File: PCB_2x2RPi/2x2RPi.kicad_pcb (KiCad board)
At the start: 2 copper layers, 44.4 x 53.3 mm, 31 parts, among them J1 USB, P1 VIN, P2 CONN_13X2, P3 INPUT, P4 REL2, P6 REL1, SW1 PWR SW, U1 LowCurVReg, U2 LowCurVReg, U3 TLP2531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

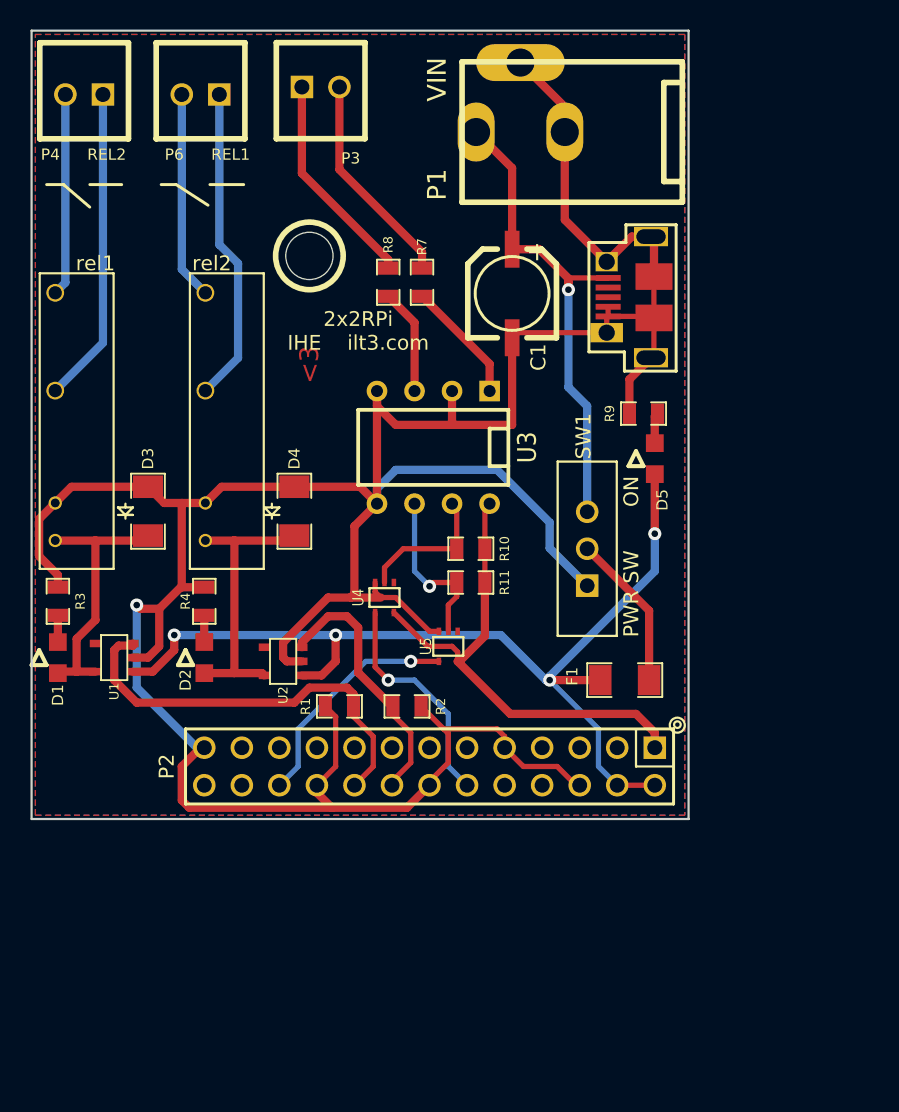
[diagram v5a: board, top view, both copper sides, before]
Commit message: Recreating schematic files, updating serial numbers
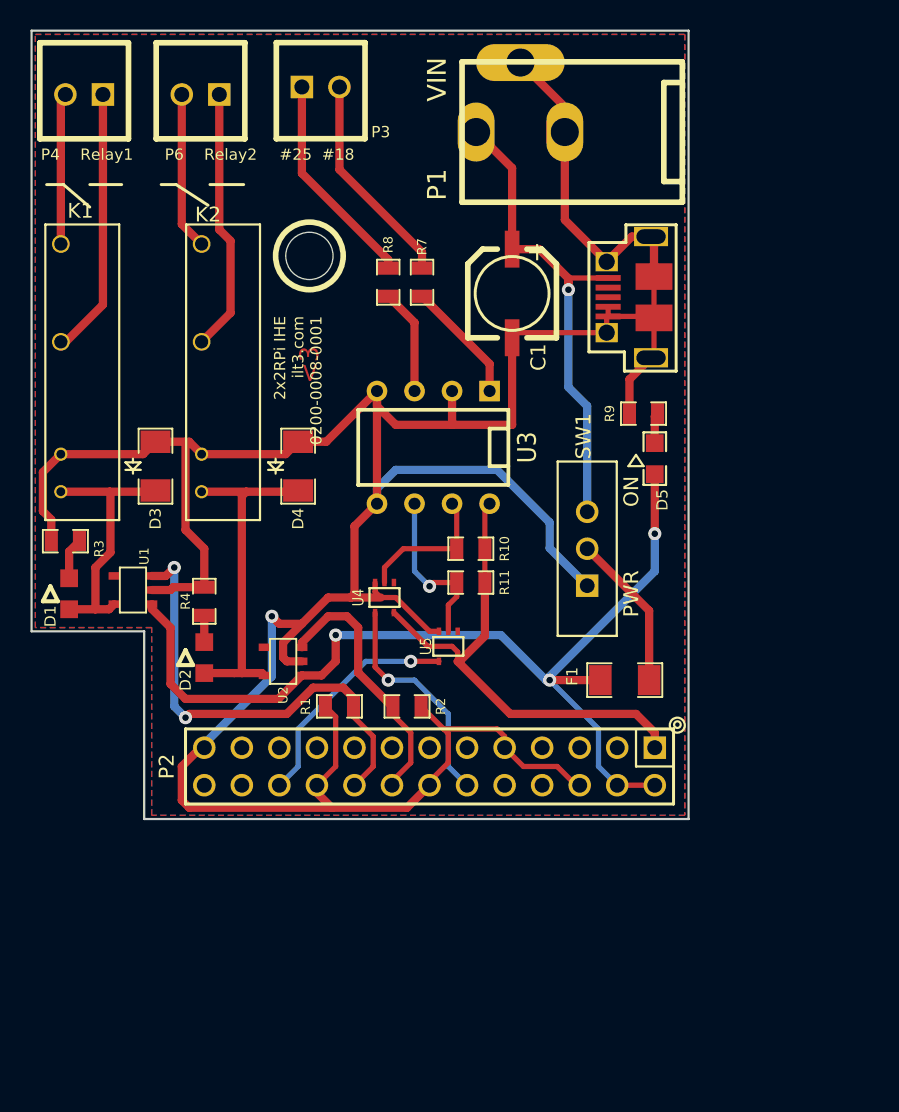
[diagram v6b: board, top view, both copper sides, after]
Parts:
- P4: value REL2 -> Relay1
- P6: value REL1 -> Relay2
- PWR IN: renamed from J1
- SW1: value PWR SW -> PWR
- moved U1 4.75 mm to (98.3, 86.9)
- moved D1 4.38 mm to (94.0, 87.1)
- moved R3 4.10 mm to (93.7, 83.6), turned to 0 degrees
- moved K1 3.32 mm to (94.9, 72.1)
- moved K2 3.31 mm to (104.4, 72.1)
- moved D3 3.09 mm to (99.8, 78.5)
- moved D4 3.06 mm to (109.5, 78.5)
- renumbered rel1 to K1, rel2 to K2
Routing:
- net /5V-Relay1: track 19.4 -> 23.1 mm
- net N-0000029: track 21.5 -> 17.9 mm
- net /GPIO_24: track 28.2 -> 31.7 mm, vias 0 -> 2
- net N-0000027: track 13.7 -> 10.2 mm
- net N-0000028: track 14.1 -> 10.7 mm
- net N-0000026: track 21.4 -> 18.1 mm
- net N-0000011: track 1.81 -> 2.80 mm
- net /5V-RPI: track 67.4 -> 67.9 mm, vias 4 -> 3
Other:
- outline, holes or cut-outs redrawn
- board text added: "2x2RPi IHE ilt3.com 0200-0008-0001"
- board text removed: "2x2RPi IHE ilt3.com"
